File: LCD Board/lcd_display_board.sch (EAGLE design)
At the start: 42 parts, among them U1 ATMEGA328P_TQFP, Y1 16MHz

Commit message: update
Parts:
- removed C7, C8: (no value), adafruit:C-USC0603
- removed ETH1: ETHERNET, ETHERNET:ETHERNET
- removed F3, F4: (no value), polyfuse:POLYFUSE
- removed H1, H2, H3, H4: MOUNT-PAD-ROUND3.6, holes:MOUNT-PAD-ROUND3.6
- removed H_INPUT: 1445055-3, con-amp:1445055-3
- removed JP4: (no value), pinhead:PINHD-1X3
- removed JP6: FTDI_DEVICE, SparkFun-Connectors:FTDI_DEVICE
- removed LED3: (no value), adafruit:LEDCHIPLED_0805
- removed R1: 10k, SparkFun-Passives:RESISTOR0603-RES
- removed R2, R3, R4: 1k, SparkFun-Resistors:RESISTOR0603-RES
- removed U$1: MQ-8MQ-8, donny_library:MQ-8MQ-8
- removed U$2: EG4621CT-ND, EG4621CT-ND:EG4621CT-ND
- removed U$3, U$9: TE770966, Shell2013:TE770966
- removed U$4: RJ9PTH, SparkFun-Connectors:RJ9PTH
- added D1: USBLC6-2SC6, USBLC6-2SC6:USBLC6-2SC6
- added F1: (no value), polyfuse:POLYFUSE
- added JP1, JP2: (no value), adafruit:PINHD-1X8BIG
- added R13, R14: 80 Ohm, SparkFun-Resistors:RESISTOR0603-RES
- C3, C6: value (none) -> 1uF; device adafruit:C-USC0603 -> adafruit:C-USC0805
- C4, C5: value (none) -> 0.1uF; device adafruit:C-USC0603 -> adafruit:C-USC0805
- LED1: value (none) -> 7-SEGMENT-4DIGIT-YOUNGSUN; device adafruit:LEDCHIPLED_0805 -> SparkFun-Displays:7-SEGMENT-4DIGIT-YOUNGSUN
- R10, R9: value 10k -> 80 Ohm; device SparkFun-Passives:RESISTOR0603-RES -> SparkFun-Resistors:RESISTOR0603-RES
- R11, R12: value 100k -> 80 Ohm
- R5: value 10k -> 1k; device SparkFun-Passives:RESISTOR0603-RES -> SparkFun-Resistors:RESISTOR0603-RES
- R6: device SparkFun-Passives:RESISTOR0603-RES -> SparkFun-Resistors:RESISTOR0603-RES
- R7, R8: value 10k -> 80 Ohm
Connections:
- removed net +12V: F3.2, H_INPUT.3, JP4.3
- removed net ESTOP1: R9.1, U$9.G/LOW, U1.PD2(INT0)
- removed net ESTOP2: R10.1, U$3.G/LOW, U1.PD3(INT1)
- removed net EXTRA_SIG: ETH1.2, R6.2, U1.PC1(ADC1)
- removed net H2OUT: R11.1, U$1.OUT, U1.PC4(ADC4/SDA)
- removed net H2OUT_2: R12.1, U1.PC5(ADC5/SCL)
- removed net H2_OK: ETH1.1, R5.2, U1.PC0(ADC0)
- removed net H2_REMOTE: H_INPUT.2, JP4.2
- removed net N$22: ETH1.LED1P
- removed net N$23: ETH1.LED1N
- removed net N$24: ETH1.LED2P
- removed net N$25: ETH1.LED2N
- removed net N$4: R3.1, U1.PC2(ADC2)
- removed net N$5: R2.1, U1.PC3(ADC3)
- removed net RXD: JP6.RXI, U1.PD0(RXD)
- removed net TARE: R8.1, U$2.P$2, U1.PD7(AIN1)
- removed net TXD: JP6.TXO, U1.PD1(TXD)
- new net DIG1AN: LED1.DIG1, U1.PC0(ADC0)
- new net DIG2AN: LED1.DIG2, U1.PC1(ADC1)
- new net DIG3AN: LED1.DIG3, U1.PC2(ADC2)
- new net DIG4AN: LED1.DIG4, U1.PC3(ADC3)
- new net N$11: R9.1, U1.PD4(XCK/T0)
- new net N$13: R11.1, U1.PD6(AIN0)
- new net N$15: R13.1, U1.PB0(ICP)
- new net N$17: D1.IO2_, JP1.3
- new net SCL: D1.IO2, U1.PC5(ADC5/SCL)
- new net SDA: D1.IO1, U1.PC4(ADC4/SDA)
- new net SEGA: LED1.A, R7.2
- new net SEGB: LED1.B, R8.2
- new net SEGC: LED1.C, R9.2
- new net SEGD: LED1.D, R10.2
- new net SEGDP: LED1.DP, R14.2
- new net SEGE: LED1.E, R11.2
- new net SEGF: LED1.F, R12.2
- new net SEGG: LED1.G, R13.2
- net +5V: now also D1.+5V, F1.1, R6.2; no longer C7.1, C8.1, F4.2, JP6.VCC, R7.2, R8.2, U$1.VCC1, U$1.VCC2, U$1.VCC3, U$3.V/SIG, U$9.V/SIG
- net ATM_RESET: now also R6.1; no longer R7.1
- net GND: now also D1.GND, JP1.4, JP1.5, JP1.6, JP1.7, JP1.8, JP2.1, JP2.2, JP2.3, JP2.4, JP2.5, JP2.6, JP2.7, JP2.8; no longer C7.2, C8.2, ETH1.5, H1.MOUNT, H2.MOUNT, H3.MOUNT, H4.MOUNT, H_INPUT.1, JP4.1, JP6.GND, LED1.C, LED3.C, R1.1, R10.2, R11.2, R12.2, R5.1, R6.1, R9.2, U$1.GND, U$2.P$1, U$4.1, U$4.2
- net N$1: now also C1.1; no longer C2.1
- net N$10: now also R8.1, U1.PD3(INT1); no longer ETH1.SHD1, ETH1.SHD2
- net N$12: now also R10.1, U1.PD5(T1); no longer F3.1, U$4.4
- net N$14: now also R12.1, U1.PD7(AIN1); no longer F4.1, U$4.3
- net N$16: now also R14.1, U1.PB1(OC1A); no longer ETH1.3
- net N$2: now also C2.1, U1.PB7(XTAL2/TOSC2), Y1.1; no longer R1.2, U$1.RL
- net N$3: now also F1.2, JP1.1; no longer C1.1, U1.PB7(XTAL2/TOSC2), Y1.1
- net N$6: now also D1.IO1_, JP1.2; no longer R4.1, U1.ADC6
- net N$7: now also R5.1, U1.ADC7; no longer LED1.A, R3.2
- net N$8: now also R5.2; no longer R2.2
- net N$9: now also R7.1, U1.PD2(INT0); no longer LED3.A, R4.2
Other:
- moved on the sheet: C1, C2, C3, C4, C5, C6, ISP1, LED2, R10, R11, R12, R5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

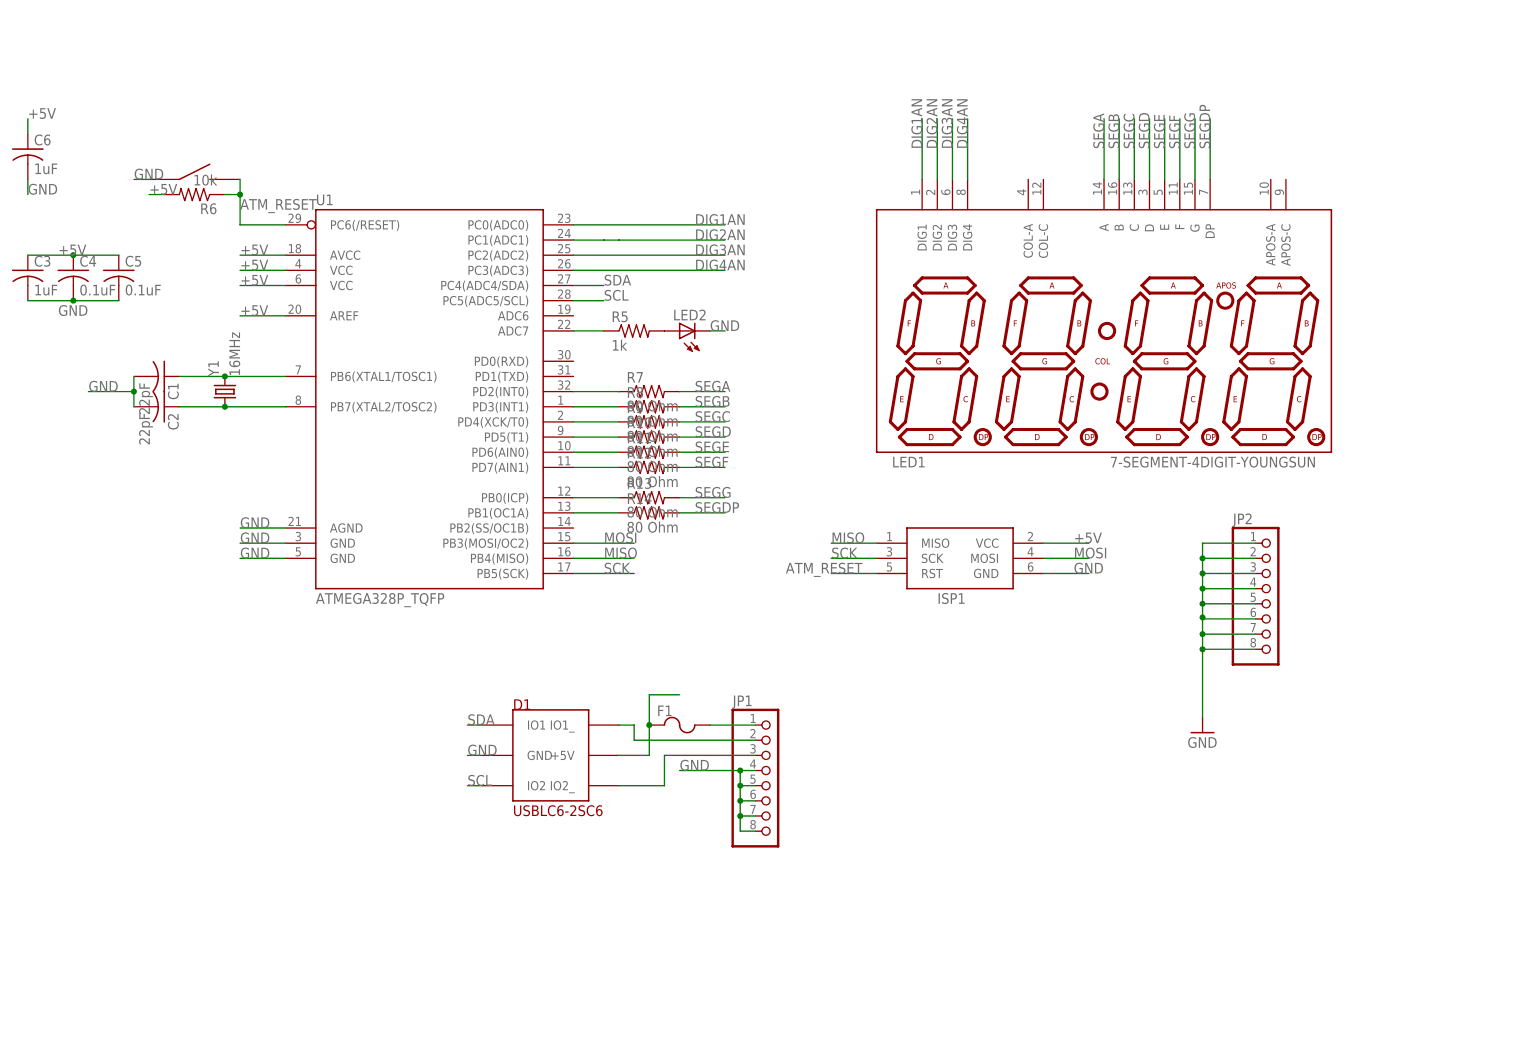
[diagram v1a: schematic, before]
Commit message: fcc schematic mostly done
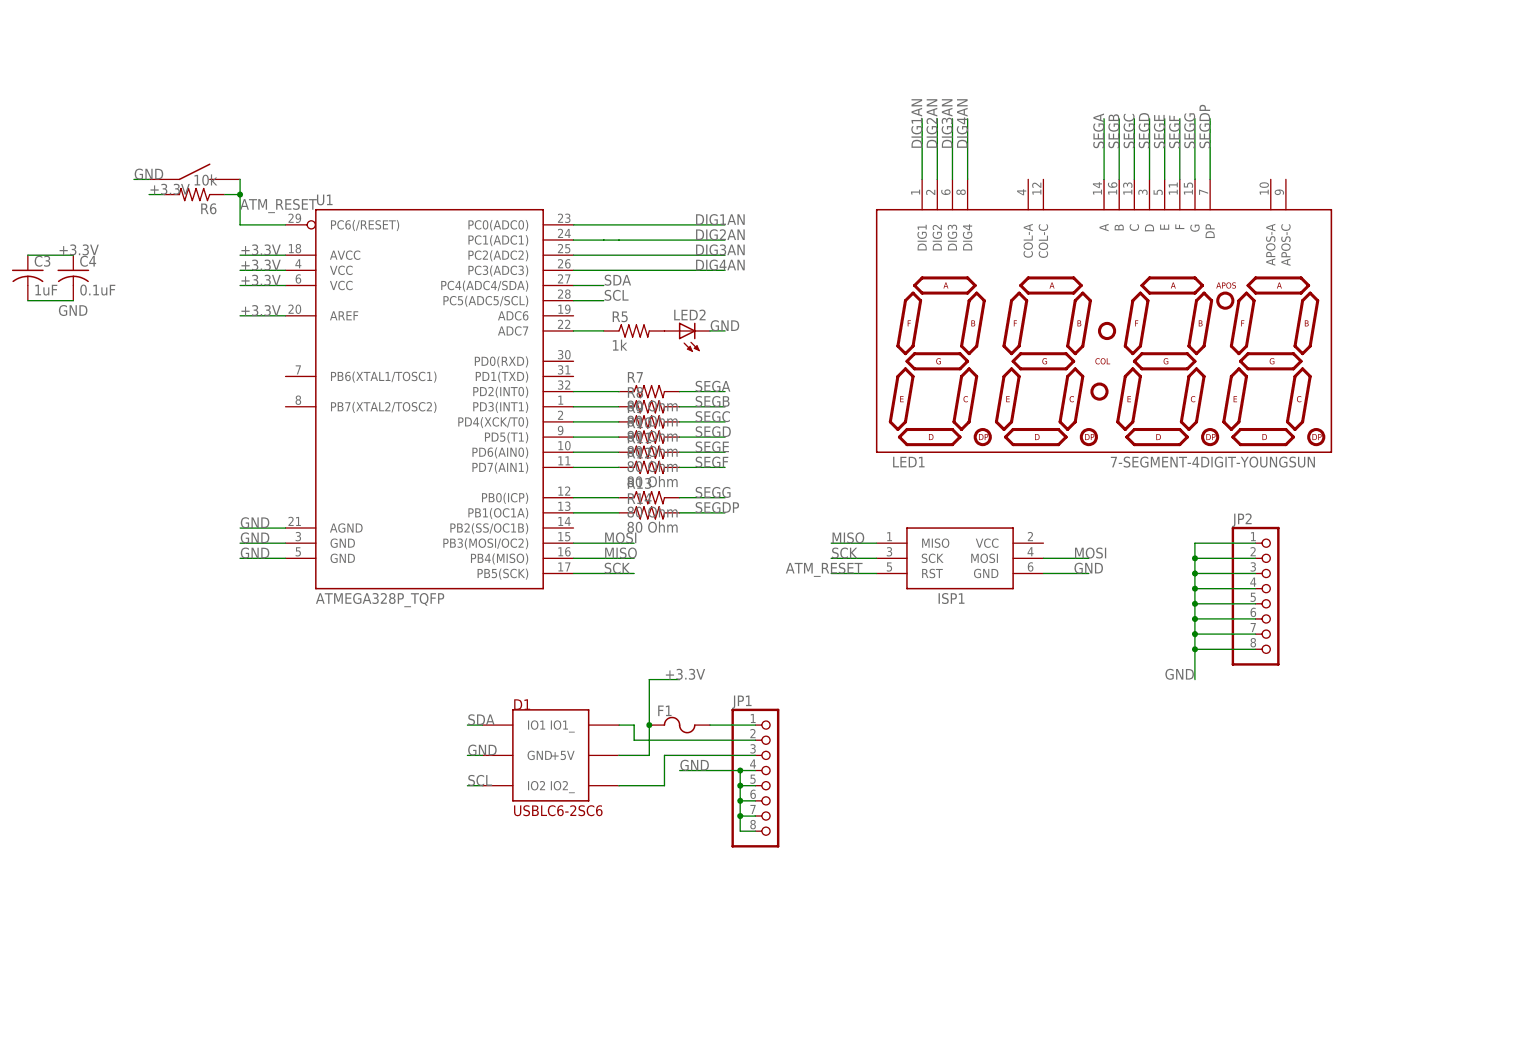
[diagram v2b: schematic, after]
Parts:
- removed C1, C2: 22pF, adafruit:C-USC0603K
- removed C5: 0.1uF, adafruit:C-USC0805
- removed C6: 1uF, adafruit:C-USC0805
- removed Y1: 16MHz, SparkFun-FreqCtrl:CRYSTALHC49US
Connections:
- removed net +5V: C3.1, C4.1, C5.1, C6.1, D1.+5V, F1.1, ISP1.VCC, R6.2, U1.AREF, U1.AVCC, U1.VCC@4, U1.VCC@6
- removed net N$1: C1.1, U1.PB6(XTAL1/TOSC1), Y1.2
- removed net N$2: C2.1, U1.PB7(XTAL2/TOSC2), Y1.1
- new net +3.3V: C3.1, C4.1, D1.+5V, F1.1, R6.2, U1.AREF, U1.AVCC, U1.VCC@4, U1.VCC@6
- net GND: no longer C1.2, C2.2, C5.2, C6.2
